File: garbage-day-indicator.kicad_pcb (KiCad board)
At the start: 2 copper layers, 46 x 63 mm, 18 parts, among them J1 Conn_01x16, J2 Conn_01x16

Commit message: Improve pcb layout
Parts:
- R1, R2, R3, R4, R5, R6, R7, R8, R9: footprint Resistor_SMD:R_0805_2012Metric -> Resistor_SMD:R_0603_1608Metric
- moved J1 0.63 mm to (107.4, 80.4)
- moved J2 0.63 mm to (130.3, 80.4)
- renumbered He1 to H2
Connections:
- J1 pad 9: /B3 -> /G1
- J2 pad 10: /G2 -> /B2
- J2 pad 11: /B2 -> /G2
- J2 pad 14: /R3 -> /R2
- J2 pad 15: /G3 -> /B1
- J2 pad 6: /G1 -> /B3
- J2 pad 7: /B1 -> /G3
- J2 pad 9: /R2 -> /R3
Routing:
- net /B3: track 58.5 -> 25.2 mm, vias 1 -> 0
- net /B1: track 31.6 -> 52.6 mm, vias 1 -> 0
- net /G3: track 47.6 -> 28.2 mm
- net /R3: track 46.2 -> 33.7 mm
- net /R2: track 37.2 -> 48.5 mm
- net /B2: track 40.2 -> 36.7 mm
- net /R1: track 17.4 -> 20.0 mm
- net /G1: track 30.7 -> 33.2 mm
- net /G2: track 38.7 -> 39.6 mm
- net Net-(D3-Pad1): track 5.63 -> 4.78 mm
- added copper zone on B.Cu, net GND
- removed copper zone on F.Cu, net GND
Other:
- board size 46 x 63 mm -> 45.9 x 62.9 mm
- board text added: "garbage-day-indicator r0 June 2022"

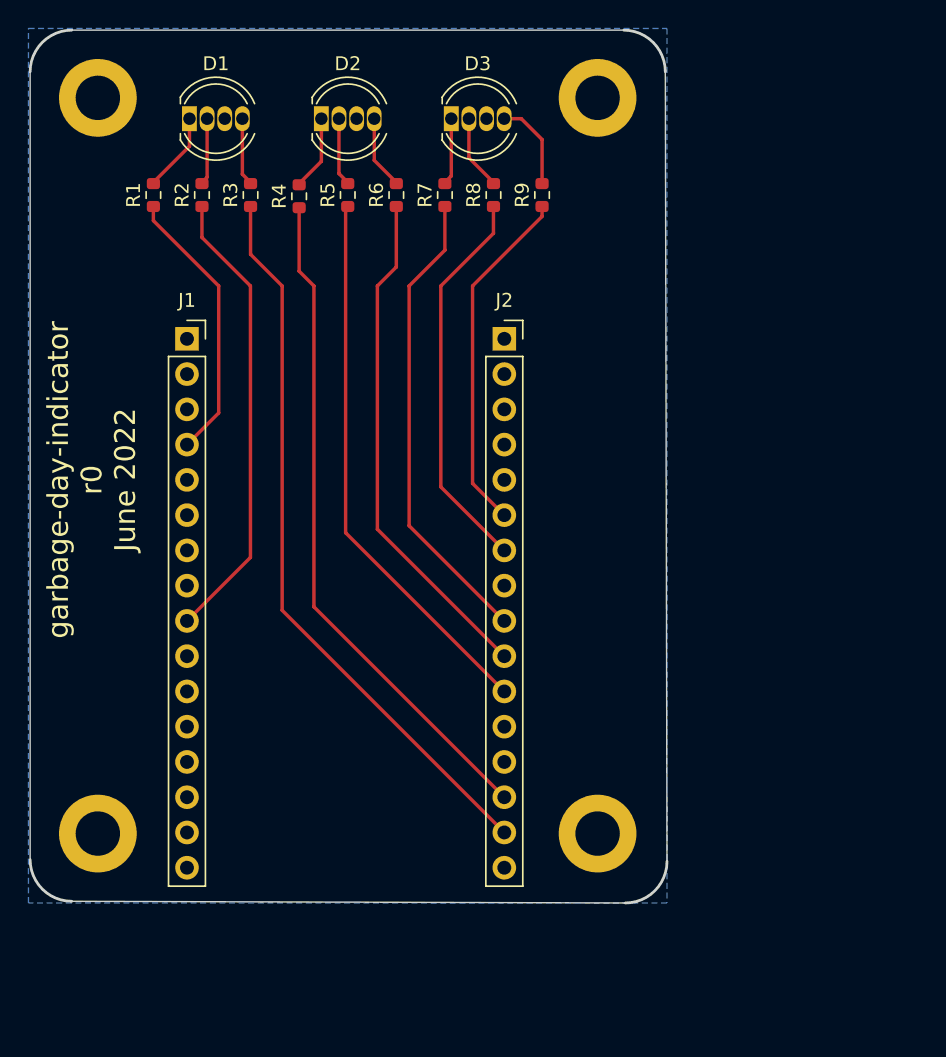
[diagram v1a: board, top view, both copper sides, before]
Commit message: Improved traces, added silkscreen revision/name
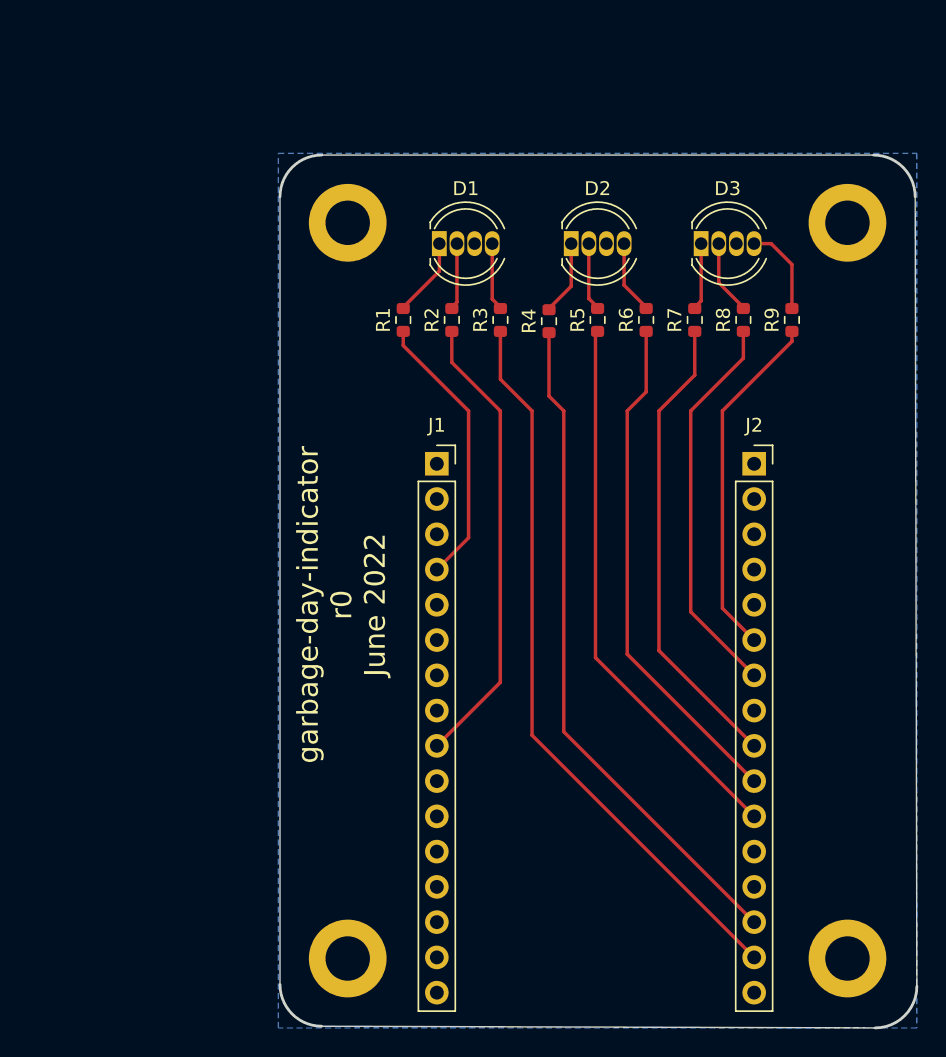
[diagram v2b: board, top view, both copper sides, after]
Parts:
- moved D3 20.1 mm to (144.5, 73.5)
- moved D1 20.1 mm to (125.6, 73.5)
- moved D2 20.1 mm to (135.1, 73.5)
- moved H1 20.1 mm to (119.0, 72.0)
- moved H2 20.1 mm to (155.0, 72.0)
- moved H3 20.1 mm to (119.0, 125.0)
- moved H4 20.1 mm to (155.0, 125.0)
- moved J1 20.1 mm to (125.4, 89.4)
- moved J2 20.1 mm to (148.3, 89.4)
- moved R1 20.1 mm to (123.0, 79.0)
- moved R2 20.1 mm to (126.5, 79.0)
- moved R3 20.1 mm to (130.0, 79.0)
- moved R4 20.1 mm to (133.5, 79.1)
- moved R5 20.1 mm to (137.0, 79.0)
- moved R6 20.1 mm to (140.5, 79.0)
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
